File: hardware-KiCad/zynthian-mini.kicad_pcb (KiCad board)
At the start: 2 copper layers, 165 x 108 mm, 39 parts, among them SW1 SW_Push, SW2 SW_Push, SW3 SW_Push, SW4 SW_Push, U1 74HCT14, U2 H11L1M

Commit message: migration to KiCad 8.0
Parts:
- G***: value MINI v1 -> MINI v2; footprint My-Library:Zynthian Logo Mask -> project-footprints:Zynthian Logo Mask

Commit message: second release
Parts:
- moved RPi1 3.29 mm to (78.0, 48.5)
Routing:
- net INTA: track 201.7 -> 0.00 mm
- net INTB: track 160.6 -> 0.00 mm, vias 1 -> 0
- net SDA: track 120.4 -> 0.00 mm
- net SCK: track 109.8 -> 0.00 mm, vias 1 -> 0
- net Net-(D1-Pad2): track 93.0 -> 6.02 mm
- net MIDI_OUT: track 82.2 -> 0.00 mm
- net ENC-SW-3: track 58.1 -> 4.43 mm
- net MIDI_IN: track 77.9 -> 37.4 mm
- net GND: track 33.6 -> 0.00 mm, vias 16 -> 0
- net Net-(MIDI-IN-J1-Pad4): track 68.3 -> 55.3 mm
- net +5V: track 274.1 -> 283.7 mm, vias 0 -> 1
- net +3.3V: track 76.5 -> 67.7 mm
- net Net-(MIDI-OUT-J1-Pad4): track 42.3 -> 33.9 mm
- net I2S_BCLK: track 78.7 -> 86.5 mm
- net I2S_LRCLK: track 50.7 -> 54.2 mm
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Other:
- outline, holes or cut-outs redrawn

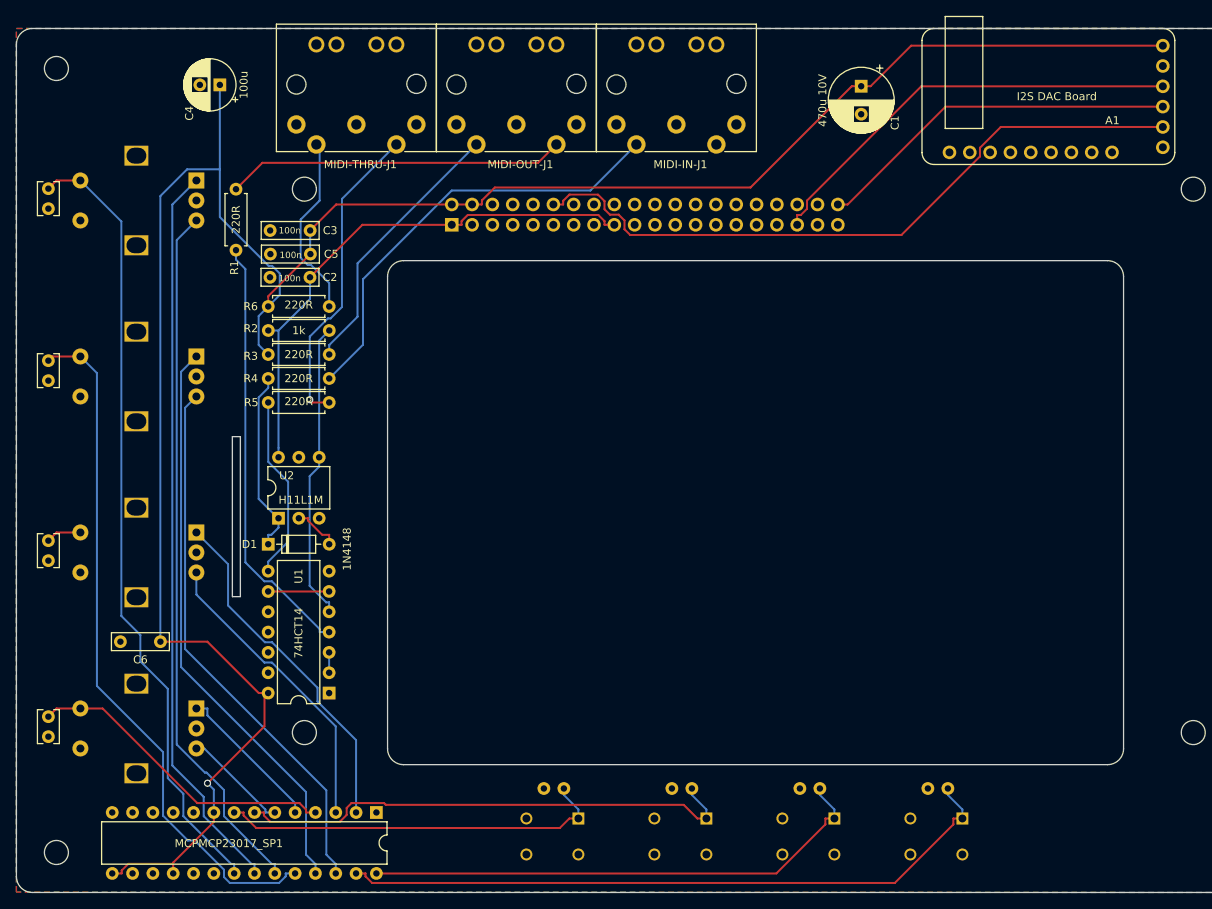
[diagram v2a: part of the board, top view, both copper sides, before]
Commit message: PCB board edge chnage
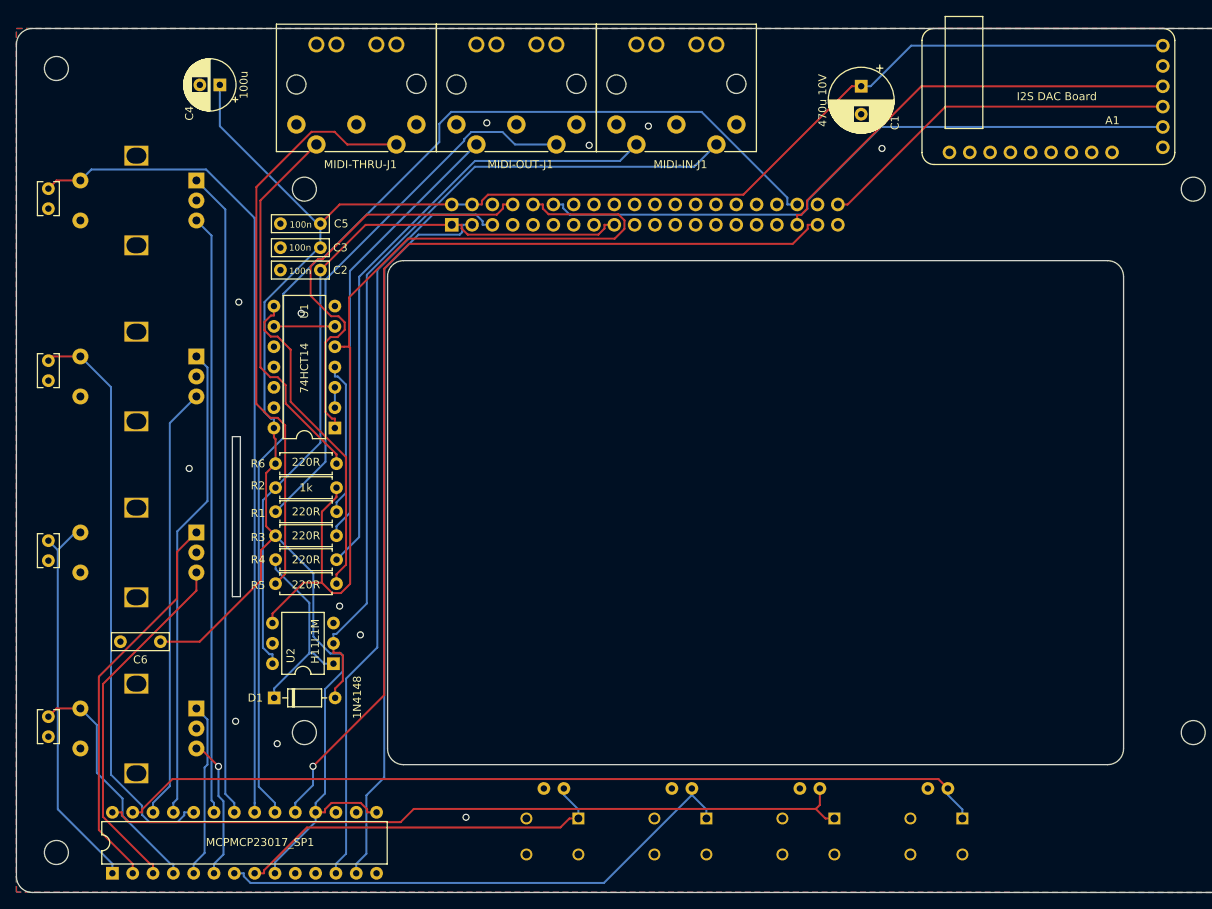
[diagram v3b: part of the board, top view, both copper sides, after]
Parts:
- moved R1 40.6 mm to (56.0, 84.4), turned to 0 degrees
- moved MCPMCP23017_SP1 33.9 mm to (35.6, 129.6), turned to 90 degrees
- moved U1 33.1 mm to (63.4, 73.9)
- moved R5 23.6 mm to (56.0, 93.4), turned to 0 degrees
- moved R4 22.7 mm to (63.6, 90.4)
- moved R3 22.7 mm to (56.0, 87.4)
- moved R6 19.7 mm to (56.0, 78.4)
- moved R2 19.7 mm to (56.0, 81.4)
- moved U2 19.4 mm to (63.2, 103.4), turned to 180 degrees
- moved D1 19.2 mm to (55.8, 107.7)
- moved C5 4.00 mm to (56.6, 48.4)
- moved C3 2.50 mm to (61.6, 51.4)
- moved C2 1.58 mm to (61.6, 54.2)
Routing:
- net INTA: track 0.00 -> 147.2 mm
- net INTB: track 0.00 -> 129.3 mm, vias 0 -> 1
- net Net-(D1-Pad2): track 6.02 -> 106.6 mm
- net SCK: track 0.00 -> 95.6 mm
- net SDA: track 0.00 -> 90.8 mm
- net MIDI_IN: track 37.4 -> 115.4 mm
- net MIDI_OUT: track 0.00 -> 53.5 mm
- net ENC-SW-3: track 4.43 -> 48.6 mm
- net Net-(R1-Pad2): track 53.8 -> 19.3 mm
- net Net-(MIDI-THRU-J1-Pad5): track 39.2 -> 73.1 mm, vias 1 -> 0
- net SWITCH-2: track 65.0 -> 94.9 mm
- net Net-(MIDI-OUT-J1-Pad5): track 42.4 -> 68.9 mm
- net +3.3V: track 67.7 -> 93.5 mm
- net Net-(MIDI-THRU-J1-Pad4): track 23.1 -> 47.3 mm
- net SWITCH-1: track 84.8 -> 108.8 mm
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
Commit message: first button layout try
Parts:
- removed G***: MINI v2, project-footprints:Zynthian Logo Mask
- added C10: 100n, Capacitor_THT:C_Rect_L4.0mm_W2.5mm_P2.50mm, F.Cu at (234.8, 65.4)
- added C11: 100n, Capacitor_THT:C_Rect_L4.0mm_W2.5mm_P2.50mm, F.Cu at (234.8, 69.4)
- added C12: 100n, Capacitor_THT:C_Rect_L4.0mm_W2.5mm_P2.50mm, B.Cu at (156.4, 136.9)
- added C14: 100n, Capacitor_THT:C_Rect_L4.0mm_W2.5mm_P2.50mm, B.Cu at (145.5, 137.1)
- added C15: 100n, Capacitor_THT:C_Rect_L4.0mm_W2.5mm_P2.50mm, B.Cu at (135.0, 137.1)
- added C17: 100n, Capacitor_THT:C_Rect_L4.0mm_W2.5mm_P2.50mm, B.Cu at (178.2, 68.8)
- added C18: 100n, Capacitor_THT:C_Rect_L4.0mm_W2.5mm_P2.50mm, B.Cu at (94.5, 118.4)
- added C20: 100n, Capacitor_THT:C_Rect_L4.0mm_W2.5mm_P2.50mm, B.Cu at (85.1, 118.4)
- added C21: 100n, Capacitor_THT:C_Rect_L4.0mm_W2.5mm_P2.50mm, B.Cu at (74.9, 118.6)
- added C23: 100n, Capacitor_THT:C_Rect_L4.0mm_W2.5mm_P2.50mm, B.Cu at (178.3, 87.9)
- added C24: 100n, Capacitor_THT:C_Rect_L4.0mm_W2.5mm_P2.50mm, B.Cu at (92.4, 137.0)
- added C25: 100n, Capacitor_THT:C_Rect_L4.0mm_W2.5mm_P2.50mm, B.Cu at (82.4, 137.0)
- added C26: 100n, Capacitor_THT:C_Rect_L4.0mm_W2.5mm_P2.50mm, B.Cu at (72.4, 137.0)
- added C27: 100n, Capacitor_THT:C_Rect_L4.0mm_W2.5mm_P2.50mm, B.Cu at (178.6, 109.5)
- added C7: 100n, Capacitor_THT:C_Rect_L7.0mm_W2.0mm_P5.00mm, F.Cu at (165.9, 104.4)
- added C8: 100n, Capacitor_THT:C_Rect_L4.0mm_W2.5mm_P2.50mm, F.Cu at (264.7, 53.8)
- added C9: 100n, Capacitor_THT:C_Rect_L4.0mm_W2.5mm_P2.50mm, F.Cu at (234.8, 61.3)
- added MCPMCP23017_SP2: MCP23017_SP, Package_DIP:DIP-28_W7.62mm, F.Cu at (164.6, 67.3)
- added R7: 10k, Resistor_THT:R_Axial_DIN0207_L6.3mm_D2.5mm_P7.62mm_Horizontal, F.Cu at (31.0, 29.0)
- added R8: 10k, Resistor_THT:R_Axial_DIN0207_L6.3mm_D2.5mm_P7.62mm_Horizontal, F.Cu at (31.0, 33.0)
- added SW10: SW_Push, project-footprints:push-button, B.Cu at (146.5, 131.7)
- added SW11: SW_Push, project-footprints:push-button, B.Cu at (136.1, 131.8)
- added SW12: SW_Push, project-footprints:push-button, B.Cu at (183.5, 69.6)
- added SW13: SW_Push, project-footprints:push-button, B.Cu at (93.6, 124.0)
- added SW14: SW_Push, project-footprints:push-button, B.Cu at (83.6, 124.0)
- added SW15: SW_Push, project-footprints:push-button, B.Cu at (73.6, 124.0)
- added SW16: SW_Push, project-footprints:push-button, B.Cu at (183.6, 89.0)
- added SW17: SW_Push, project-footprints:push-button, B.Cu at (93.6, 132.0)
- added SW18: SW_Push, project-footprints:push-button, B.Cu at (83.6, 132.0)
- added SW19: SW_Push, project-footprints:push-button, B.Cu at (73.6, 132.0)
- added SW20: SW_Push, project-footprints:push-button, B.Cu at (183.6, 111.0)
- added SW5: SW_Push, project-footprints:push-button, F.Cu at (267.6, 60.2)
- added SW6: SW_Push, project-footprints:push-button, F.Cu at (268.0, 70.4)
- added SW7: SW_Push, project-footprints:push-button, F.Cu at (238.4, 43.9)
- added SW8: SW_Push, project-footprints:push-button, F.Cu at (238.4, 51.5)
- added SW9: SW_Push, project-footprints:push-button, B.Cu at (157.6, 131.8)
- moved SW4 105.1 mm to (133.6, 29.1)
- moved SW3 104.1 mm to (147.3, 29.1)
- moved SW2 103.3 mm to (161.0, 29.1)
- moved SW1 102.4 mm to (174.8, 29.1)
- moved C34 94.9 mm to (135.0, 34.4)
- moved C33 93.9 mm to (148.8, 34.4)
- moved C32 92.9 mm to (162.5, 34.4)
- moved C31 92.0 mm to (176.2, 34.4)
- moved REF** 76.0 mm to (149.0, 46.8)
- moved C1 16.5 mm to (137.6, 45.4)
- moved A1 13.3 mm to (139.3, 32.4)
- moved MCPMCP23017_SP1 4.62 mm to (33.3, 133.6)
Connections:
- D1 pad 1: Net-(D1-Pad1) -> (no net)
- D1 pad 2: Net-(D1-Pad2) -> (no net)
- MCPMCP23017_SP1 pad 1: ENC-SW-3 -> ENC-A-1
- MCPMCP23017_SP1 pad 11: unconnected-(MCPMCP23017_SP1-Pad11) -> (no net)
- MCPMCP23017_SP1 pad 14: unconnected-(MCPMCP23017_SP1-Pad14) -> (no net)
- MCPMCP23017_SP1 pad 19: INTB -> (no net)
- MCPMCP23017_SP1 pad 2: ENC-A-3 -> ENC-B-1
- MCPMCP23017_SP1 pad 20: INTA -> (no net)
- MCPMCP23017_SP1 pad 21: ENC-SW-1 -> SWITCH-17
- MCPMCP23017_SP1 pad 22: ENC-A-1 -> SWITCH-18
- MCPMCP23017_SP1 pad 23: ENC-B-1 -> SWITCH-19
- MCPMCP23017_SP1 pad 24: ENC-SW-2 -> SWITCH-20
- MCPMCP23017_SP1 pad 25: ENC-A-2 -> ENC-SW-1
- MCPMCP23017_SP1 pad 26: ENC-B-2 -> ENC-SW-2
- MCPMCP23017_SP1 pad 27: SWITCH-1 -> ENC-SW-3
- MCPMCP23017_SP1 pad 28: SWITCH-2 -> ENC-SW-4
- MCPMCP23017_SP1 pad 3: ENC-B-3 -> ENC-A-2
- MCPMCP23017_SP1 pad 4: ENC-SW-4 -> ENC-B-2
- MCPMCP23017_SP1 pad 5: ENC-A-4 -> ENC-A-3
- MCPMCP23017_SP1 pad 6: ENC-B-4 -> ENC-B-3
- MCPMCP23017_SP1 pad 7: SWITCH-3 -> ENC-A-4
- MCPMCP23017_SP1 pad 8: SWITCH-4 -> ENC-B-4
- MIDI-IN-J1 pad 5: Net-(D1-Pad2) -> Net-(D1-A)
- R4 pad 2: Net-(D1-Pad1) -> Net-(D1-K)
- RPi1 pad 11: unconnected-(RPi1-Pad11) -> INT3
- RPi1 pad 13: unconnected-(RPi1-Pad13) -> INT4
- RPi1 pad 15: unconnected-(RPi1-Pad15) -> (no net)
- RPi1 pad 16: unconnected-(RPi1-Pad16) -> (no net)
- RPi1 pad 18: unconnected-(RPi1-Pad18) -> (no net)
- RPi1 pad 19: unconnected-(RPi1-Pad19) -> (no net)
- RPi1 pad 21: unconnected-(RPi1-Pad21) -> (no net)
- RPi1 pad 22: unconnected-(RPi1-Pad22) -> (no net)
- RPi1 pad 23: unconnected-(RPi1-Pad23) -> (no net)
- RPi1 pad 24: unconnected-(RPi1-Pad24) -> (no net)
- RPi1 pad 26: unconnected-(RPi1-Pad26) -> (no net)
- RPi1 pad 27: unconnected-(RPi1-Pad27) -> (no net)
- RPi1 pad 28: unconnected-(RPi1-Pad28) -> (no net)
- RPi1 pad 29: unconnected-(RPi1-Pad29) -> INT1
- RPi1 pad 31: unconnected-(RPi1-Pad31) -> INT2
- RPi1 pad 32: unconnected-(RPi1-Pad32) -> (no net)
- RPi1 pad 33: unconnected-(RPi1-Pad33) -> (no net)
- RPi1 pad 36: INTA -> (no net)
- RPi1 pad 37: INTB -> (no net)
- RPi1 pad 38: unconnected-(RPi1-Pad38) -> (no net)
- RPi1 pad 7: unconnected-(RPi1-Pad7) -> (no net)
- U2 pad 1: Net-(D1-Pad1) -> Net-(D1-K)
- U2 pad 2: Net-(D1-Pad2) -> Net-(D1-A)
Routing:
- net +5V: track 262.4 -> 0.00 mm
- net INTA: track 147.2 -> 0.00 mm
- net INTB: track 129.3 -> 0.00 mm, vias 1 -> 0
- net MIDI_IN: track 115.4 -> 0.00 mm
- net SWITCH-1: track 108.8 -> 0.00 mm
- net Net-(D1-Pad2): track 106.6 -> 0.00 mm
- net ENC-SW-1: track 103.6 -> 0.00 mm
- net SCK: track 95.6 -> 0.00 mm
- net SWITCH-2: track 94.9 -> 0.00 mm
- net +3.3V: track 93.5 -> 0.00 mm
- net SDA: track 90.8 -> 0.00 mm
- net I2S_BCLK: track 82.1 -> 0.00 mm
- net ENC-A-1: track 80.9 -> 0.00 mm
- net Net-(MIDI-IN-J1-Pad4): track 78.0 -> 0.00 mm
- net ENC-B-1: track 74.9 -> 0.00 mm
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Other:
- board size 165 x 108 mm -> 165 x 115 mm

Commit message: work on PCB switches and CAD
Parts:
- MCPMCP23017_SP2: moved to B.Cu
- moved MCPMCP23017_SP2 30.2 mm to (164.6, 97.5)
- moved C26 19.3 mm to (83.1, 121.0)
- moved C18 15.3 mm to (109.4, 122.0)
- moved SW13 14.8 mm to (108.1, 127.0)
- moved C20 11.7 mm to (96.6, 120.0), turned to 90 degrees
- moved SW19 11.6 mm to (84.1, 127.0), turned to -90 degrees
- moved C15 10.1 mm to (145.1, 137.0)
- moved SW11 10.1 mm to (146.1, 132.0)
- moved SW10 9.65 mm to (156.1, 132.0)
- moved C14 9.65 mm to (155.1, 137.0)
- moved C12 8.80 mm to (165.2, 137.0)
- moved SW9 8.77 mm to (166.4, 132.0)
- moved C24 8.06 mm to (99.4, 133.0), turned to 180 degrees
- moved SW14 7.76 mm to (91.1, 122.0), turned to 90 degrees
- moved SW18 7.50 mm to (91.1, 132.0), turned to -90 degrees
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
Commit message: first usable v2-20-buttons version
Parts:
- C10, C11, C7, C8, C9, SW5, SW6, SW7, SW8: moved to B.Cu
- Enc1, Enc2, Enc3, Enc4: footprint Rotary_Encoder:RotaryEncoder_Alps_EC12E-Switch_Vertical_H20mm -> project-footprints:RotaryEncoder_Alps_EC12E-Switch_Vertical_H20mm
- moved SW6 124.0 mm to (156.1, 124.0), turned to 180 degrees
- moved SW7 122.2 mm to (146.1, 124.0), turned to 180 degrees
- moved C8 115.7 mm to (174.9, 126.8), turned to -90 degrees
- moved SW5 109.8 mm to (181.1, 128.0), turned to 180 degrees
- moved C10 102.8 mm to (147.2, 119.1), turned to 180 degrees
- moved C9 96.6 mm to (157.3, 119.0), turned to 180 degrees
- moved C11 62.9 mm to (177.1, 44.5), turned to -90 degrees
- moved SW8 56.6 mm to (182.1, 45.5), turned to -90 degrees
- moved REF** 31.7 mm to (178.3, 34.6)
- moved C31 11.9 mm to (164.9, 37.9), turned to 0 degrees
- moved R7 11.6 mm to (41.0, 34.8), turned to 180 degrees
- moved R8 10.3 mm to (41.0, 30.8), turned to 180 degrees
- moved C33 9.35 mm to (144.9, 25.9), turned to 0 degrees
- moved SW1 9.11 mm to (166.1, 32.0), turned to -90 degrees
- moved C34 8.50 mm to (135.2, 25.9), turned to 0 degrees
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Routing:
- net +5V: track 0.00 -> 334.1 mm
- net SCK: track 0.00 -> 298.9 mm, vias 0 -> 1
- net SDA: track 0.00 -> 292.9 mm, vias 0 -> 3
- net SWITCH-15: track 0.00 -> 155.6 mm
- net SWITCH-20: track 0.00 -> 145.2 mm
- net +3.3V: track 0.00 -> 135.4 mm
- net Net-(MIDI-THRU-J1-Pad5): track 0.00 -> 107.7 mm
- net Net-(D1-A): track 0.00 -> 106.8 mm
- net SWITCH-14: track 0.00 -> 105.8 mm
- net ENC-A-1: track 0.00 -> 98.5 mm
- net SWITCH-13: track 0.00 -> 93.8 mm
- net SWITCH-3: track 0.00 -> 92.1 mm
- net ENC-SW-1: track 0.00 -> 91.2 mm
- net ENC-B-1: track 0.00 -> 89.9 mm
- net SWITCH-4: track 0.00 -> 87.4 mm, vias 0 -> 1
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
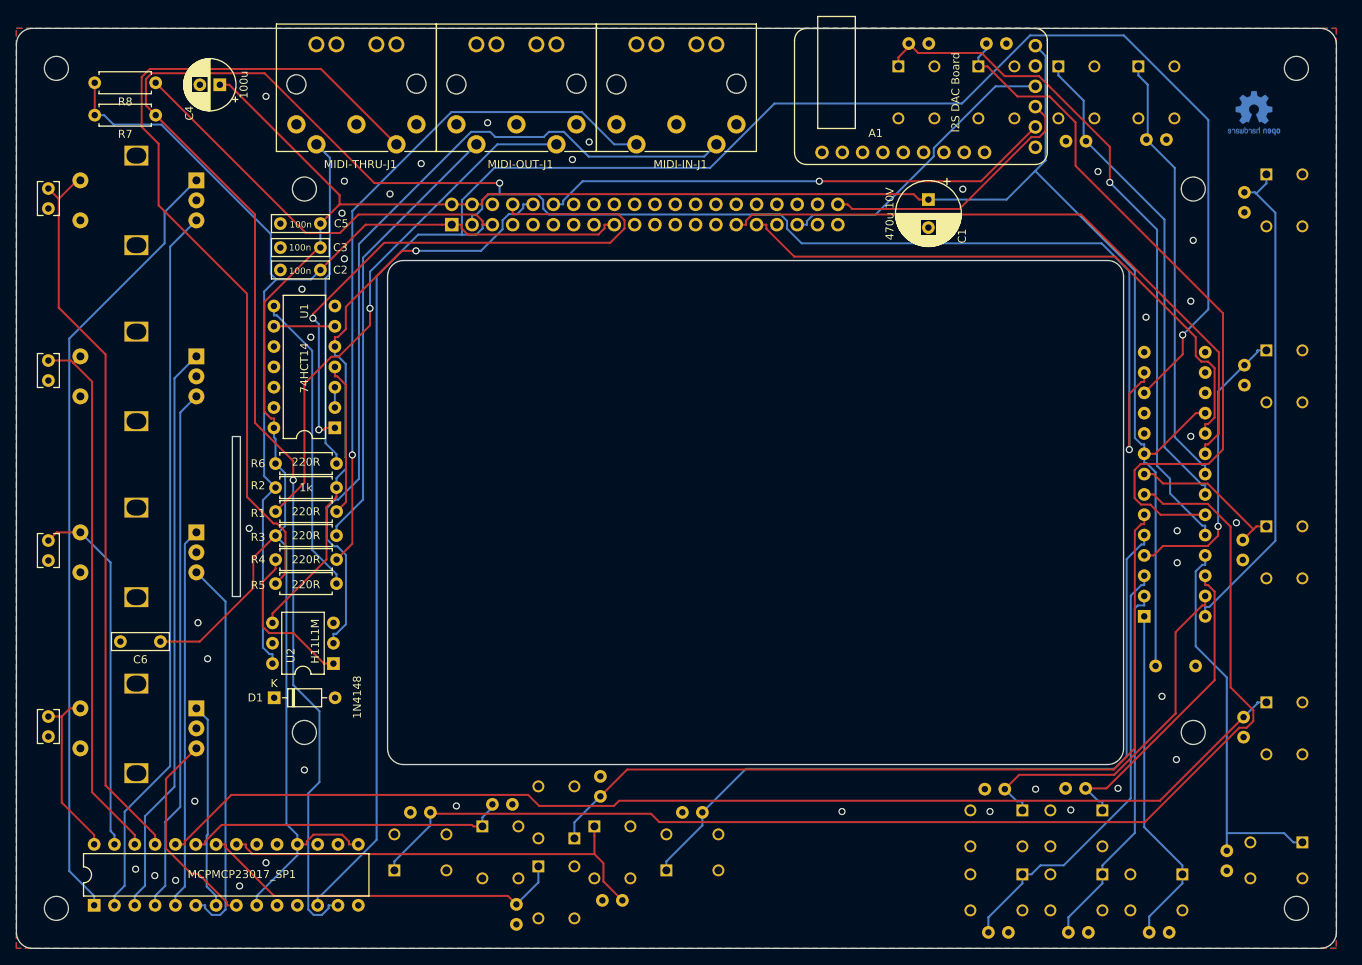
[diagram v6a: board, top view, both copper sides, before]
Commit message: making space for rpi4
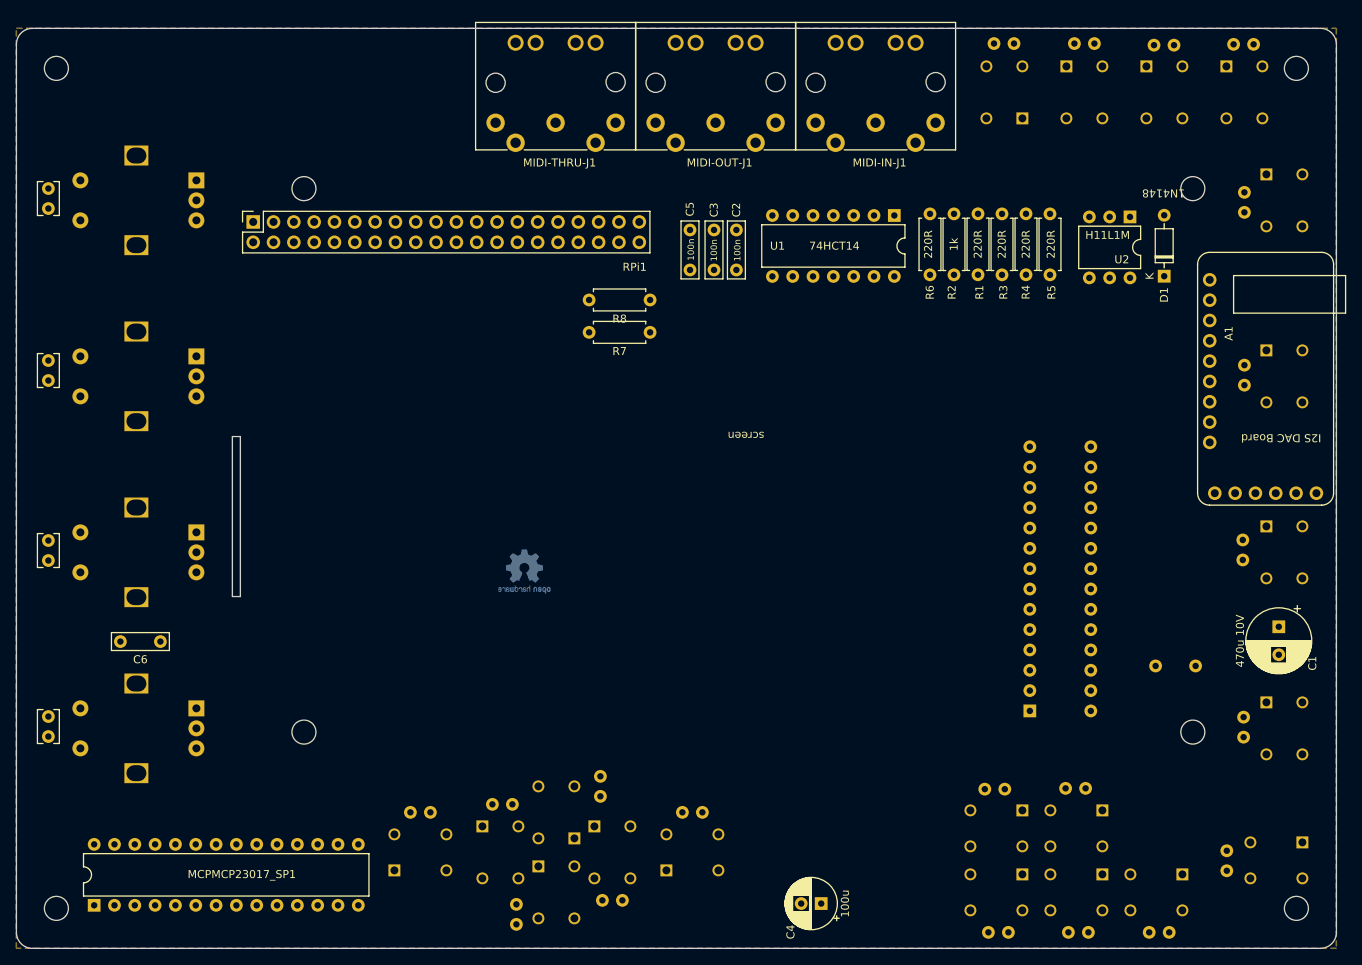
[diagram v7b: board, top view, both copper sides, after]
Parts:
- added screen: aliexpress 5 inch screen, project-footprints:aliexpress 5 inch screen, F.Cu at (115.1, 78.0)
- RPi1: moved to F.Cu
- moved C4 127.0 mm to (124.2, 133.4)
- moved D1 123.1 mm to (167.1, 55.0), turned to 90 degrees
- moved U2 114.2 mm to (162.8, 47.5), turned to -90 degrees
- moved REF** 107.7 mm to (87.1, 91.9)
- moved R5 104.2 mm to (152.8, 54.8), turned to 90 degrees
- moved R3 96.5 mm to (146.8, 54.8), turned to 90 degrees
- moved R4 96.4 mm to (149.8, 47.2), turned to -90 degrees
- moved R1 92.7 mm to (143.8, 54.8), turned to 90 degrees
- moved R2 88.9 mm to (140.8, 54.8), turned to 90 degrees
- moved R6 85.1 mm to (137.8, 54.8), turned to 90 degrees
- moved U1 74.8 mm to (133.3, 47.4), turned to -90 degrees
- moved C1 69.1 mm to (181.4, 98.8)
- moved R7 67.5 mm to (102.8, 62.0)
- moved R8 67.5 mm to (102.8, 57.9)
- moved A1 55.7 mm to (179.8, 67.8), turned to 90 degrees
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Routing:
- net +5V: track 334.1 -> 0.00 mm
- net SCK: track 298.9 -> 0.00 mm, vias 1 -> 0
- net SDA: track 292.9 -> 0.00 mm, vias 3 -> 0
- net SWITCH-15: track 155.6 -> 0.00 mm
- net SWITCH-20: track 145.2 -> 0.00 mm
- net +3.3V: track 135.4 -> 0.00 mm
- net Net-(MIDI-THRU-J1-Pad5): track 107.7 -> 0.00 mm
- net Net-(D1-A): track 106.8 -> 0.00 mm
- net SWITCH-14: track 105.8 -> 0.00 mm
- net ENC-A-1: track 98.5 -> 0.00 mm
- net SWITCH-13: track 93.8 -> 0.00 mm
- net SWITCH-3: track 92.1 -> 0.00 mm
- net ENC-SW-1: track 91.2 -> 0.00 mm
- net ENC-B-1: track 89.9 -> 0.00 mm
- net SWITCH-4: track 87.4 -> 0.00 mm, vias 1 -> 0
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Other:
- outline, holes or cut-outs redrawn
